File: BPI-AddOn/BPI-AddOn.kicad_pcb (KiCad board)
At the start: 2 copper layers, 100 x 100 mm, 81 parts, among them CON1 BARREL_JACK, J1 RJ45, J2 RJ45, J3 RJ45, P1 DIN10-1, P10 CONN_01X03, P11 CONN_01X05, P12 CONN_01X05, P13 CONN_01X08, P15 CONN_02X11, P16 USB_B, P17 CONN_01X05, P18 CONN_01X05, P19 V, P2 DIN10-2, P20 - +, P21 USB_OTG, P22 CONN_01X06, P23 CONN_01X06, P24 CONN_02X02, P25 CONN_01X02, P3 DIN10-3, P4 DIN10-4, P5 DIN10-5, P6 DIN7-1, P7 DIN7-2, P8 DIN7-3, P9 CONN_01X03, U1 MC34063, U2 FT230XS

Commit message: wip
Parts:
- added G***: LOGO, w_logo:Logo_copper_CC-BY-NC-SA_10x3.6mm, F.Cu at (91.5, 101.5)
- added G***: LOGO, w_logo:Logo_copper_CC-BY-NC-SA_10x3.6mm, F.Cu at (133.5, 113.5)
- added G***: LOGO, w_logo:Logo_copper_CC-BY-NC-SA_10x3.6mm, F.Cu at (160.0, 136.5)
- moved REF3 1.41 mm to (162.0, 144.0)
- moved REF4 1.41 mm to (127.0, 144.0)
- moved REF3 1.12 mm to (127.0, 129.0)
- moved REF4 1.12 mm to (162.0, 129.0)
- moved P21 0.50 mm to (144.5, 118.0)
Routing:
- net /GSB: track 0.00 -> 62.9 mm
- net VCC: track 130.6 -> 124.4 mm
- net /CANL: track 131.3 -> 126.7 mm
- net /CANH: track 133.9 -> 130.7 mm
- added copper zone on B.Cu, net GNDA
- added copper zone on F.Cu, net GNDA
- added copper zone on B.Cu, net GNDD
- added copper zone on F.Cu, net GNDD
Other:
- board text added: "Version 1.0 06/2016 Gerhard Bertelsmann"

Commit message: wip
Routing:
- net /GS0: track 45.8 -> 152.0 mm
- net /GSB: track 62.9 -> 141.9 mm
- net VCC: track 124.4 -> 176.6 mm
- net /CANH: track 130.7 -> 181.6 mm
- net /CANL: track 126.7 -> 175.9 mm
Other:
- net class Defaul_II: clearance 0.2 -> 0.4
- net class Default: clearance 0.2 -> 0.4
- rule trace_clearance: 0.2 -> 0.4

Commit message: route left part ...
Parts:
- CON1: value BARREL_JACK -> BJ
- moved F1 1.13 mm to (92.6, 68.0)
- moved D4 0.27 mm to (98.5, 83.2), turned to 90 degrees
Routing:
- net /CANH: track 181.6 -> 288.9 mm, vias 2 -> 11
- net /CANL: track 175.9 -> 256.0 mm, vias 2 -> 11
- net /5V: track 25.7 -> 102.8 mm, vias 0 -> 1
- net /GSB: track 141.9 -> 215.7 mm, vias 0 -> 1
- net /GS0: track 152.0 -> 219.6 mm, vias 0 -> 7
- net VCC: track 176.6 -> 239.6 mm, vias 1 -> 7
- net Net-(F2-Pad1): track 0.00 -> 25.4 mm, vias 0 -> 1
- net Net-(P19-Pad3): track 0.00 -> 18.7 mm
- net Net-(P16-Pad5): track 0.00 -> 16.6 mm, vias 0 -> 2
- net Net-(J2-Pad9): track 0.00 -> 15.5 mm
- net Net-(J1-Pad9): track 0.00 -> 15.5 mm
- net Net-(F1-Pad2): track 0.00 -> 14.2 mm
- net Net-(CON1-Pad3): track 0.00 -> 9.39 mm
- net /Vdd: track 0.00 -> 7.47 mm
- net Net-(P25-Pad1): track 0.00 -> 6.54 mm
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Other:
- net class Defaul_II: clearance 0.4 -> 0.2
- net class Default: clearance 0.4 -> 0.2
- rule trace_clearance: 0.4 -> 0.2
- board text added: "AK"
- board text added: "BJ"

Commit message: wip
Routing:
- net VCC: track 239.6 -> 261.5 mm, vias 7 -> 9
- net /GS0: track 219.6 -> 223.3 mm
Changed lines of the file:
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@@
-(kicad_pcb (version 4) (host pcbnew 4.0.2-stable)
+(kicad_pcb (version 4) (host pcbnew 4.0.1-stable)
   (general
     (links 233)
-    (no_connects 113)
-    (area 66.924999 48.924999 167.075001 149.075001)
+    (no_connects 140)
+    (area 64.132499 38.02446 183.5 159.200001)
     (thickness 1.6)
     (drawings 90)
-    (tracks 380)
+    (tracks 393)
     (zones 0)
     (modules 84)
@@
   (gr_line (start 69.5 149) (end 114.5 149) (angle 90) (layer Edge.Cuts) (width 0.15))
   (gr_line (start 69.5 49) (end 114.5 49) (angle 90) (layer Edge.Cuts) (width 0.15))
+  (segment (start 75.5 121.65) (end 79.1685 121.65) (width 0.6) (layer F.Cu) (net 1) (status 400000))
+  (segment (start 79.1685 121.65) (end 79.1845 121.666) (width 0.6) (layer F.Cu) (net 1))
   (segment (start 82.50249 73.063905) (end 82.50249 73.771011) (width 0.6) (layer F.Cu) (net 1))
   (segment (start 82.486589 66.431589) (end 82.486589 73.048004) (width 0.6) (layer F.Cu) (net 1))
@@
   (segment (start 96.6724 60.1599) (end 100.6729 56.1594) (width 1.2) (layer B.Cu) (net 11))
   (segment (start 95.0976 68.0466) (end 96.6724 66.4718) (width 1.2) (layer B.Cu) (net 11))
-  (segment (start 92.8878 70.739) (end 90.551 73.0758) (width 1.2) (layer F.Cu) (net 12))
-  (segment (start 90.551 73.0758) (end 90.551 87.0585) (width 1.2) (layer F.Cu) (net 12))
-  (segment (start 91.96 63) (end 91.96 69.8112) (width 1.2) (layer B.Cu) (net 12))
-  (segment (start 91.96 69.8112) (end 92.8878 70.739) (width 1.2) (layer B.Cu) (net 12))
-  (via (at 92.8878 70.739) (size 1.3) (drill 1) (layers F.Cu B.Cu) (net 12))
+  (segment (start 92.839655 69.337481) (end 93.489654 69.98748) (width 1.2) (layer B.Cu) (net 12))
+  (segment (start 91.96 63) (end 91.96 68.457826) (width 1.2) (layer B.Cu) (net 12))
+  (segment (start 92.839655 70.637479) (end 93.489654 69.98748) (width 1.2) (layer F.Cu) (net 12))
+  (segment (start 90.551 72.926134) (end 92.839655 70.637479) (width 1.2) (layer F.Cu) (net 12))
+  (segment (start 90.551 87.0585) (end 90.551 72.926134) (width 1.2) (layer F.Cu) (net 12))
+  (segment (start 91.96 68.457826) (end 92.839655 69.337481) (width 1.2) (layer B.Cu) (net 12))
+  (via (at 93.489654 69.98748) (size 1.3) (drill 1) (layers F.Cu B.Cu) (net 12))
   (segment (start 85.217 91.8845) (end 87.757 91.8845) (width 1.2) (layer B.Cu) (net 13))
   (segment (start 85.217 91.8845) (end 85.217 87.3125) (width 1.2) (layer B.Cu) (net 13))
@@
   (segment (start 152.78 134.72) (end 152.78 126.5) (width 0.6) (layer B.Cu) (net 20))
   (segment (start 150.38 137.12) (end 152.78 134.72) (width 0.6) (layer B.Cu) (net 20))
+  (segment (start 94.8055 71.4375) (end 94.8055 75.071022) (width 1.2) (layer F.Cu) (net 22))
+  (via (at 94.8055 75.071022) (size 1.3) (drill 1) (layers F.Cu B.Cu) (net 22))
+  (segment (start 94.8055 71.4375) (end 97.9805 71.4375) (width 1.2) (layer B.Cu) (net 22))
+  (segment (start 86.0439 71.4375) (end 94.8055 71.4375) (width 1.2) (layer B.Cu) (net 22))
+  (via (at 94.8055 71.4375) (size 1.3) (drill 1) (layers F.Cu B.Cu) (net 22))
+  (segment (start 97.9805 71.4375) (end 98.75 70.668) (width 1.2) (layer B.Cu) (net 22))
+  (segment (start 98.75 70.668) (end 98.75 68.58) (width 1.2) (layer B.Cu) (net 22))
+  (segment (start 85.25 68.58) (end 85.25 70.6436) (width 1.2) (layer B.Cu) (net 22))
+  (segment (start 85.25 70.6436) (end 86.0439 71.4375) (width 1.2) (layer B.Cu) (net 22))
   (segment (start 98.5012 83.185) (end 103.117233 83.185) (width 1.2) (layer F.Cu) (net 22))
   (segment (start 103.117233 83.185) (end 104.057033 82.2452) (width 1.2) (layer F.Cu) (net 22))

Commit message: wip
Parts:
- added P14: CONN_02X11, Pin_Headers:Pin_Header_Straight_2x11, F.Cu at (127.3, 85.5)
- CON1: value BJ -> BARREL_JACK
- moved C8 28.4 mm to (156.2, 103.9), turned to 0 degrees
- moved C9 26.0 mm to (156.2, 106.7), turned to 0 degrees
- moved U2 21.6 mm to (156.1, 111.0)
- moved R12 18.7 mm to (151.3, 112.3), turned to 90 degrees
- moved C5 10.5 mm to (149.7, 104.5)
- moved P23 10.4 mm to (125.5, 99.4)
- moved R10 7.04 mm to (152.9, 119.0), turned to 180 degrees
- moved R11 5.17 mm to (152.9, 115.8), turned to 180 degrees
- moved D2 4.47 mm to (157.7, 119.0), turned to 0 degrees
- moved G*** 1.76 mm to (133.0, 111.8)
- moved D3 1.41 mm to (157.7, 115.8), turned to 0 degrees
- moved E05 0.61 mm to (145.0, 120.0)
- moved E05 0.41 mm to (145.0, 122.5)
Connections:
- net /Vout renamed /21_15
- net Net-(P15-Pad1) renamed /21_01
- net Net-(P15-Pad3) renamed /21_02
- C2 pad 1: VCC -> VAA
- D4 pad 1: VCC -> /Vcc
- P1 pad 1: VCC -> /Vcc
- P1 pad 5: VCC -> /Vcc
- P10 pad 3: VCC -> /Vcc
- P11 pad 1: VCC -> /Vcc
- P12 pad 1: VCC -> /Vcc
- P15 pad 10: Net-(P15-Pad10) -> /21_17
- P15 pad 11: Net-(P15-Pad11) -> /21_06
- P15 pad 12: Net-(P15-Pad12) -> /21_16
- P15 pad 13: Net-(P15-Pad13) -> /21_07
- P15 pad 15: Net-(P15-Pad15) -> /21_08
- P15 pad 16: Net-(P15-Pad16) -> /21_14
- P15 pad 17: Net-(P15-Pad17) -> /21_09
- P15 pad 18: Net-(P15-Pad18) -> /21_13
- P15 pad 19: Net-(P15-Pad19) -> /21_10
- P15 pad 20: Net-(P15-Pad20) -> /21_12
- P15 pad 22: Net-(P15-Pad22) -> /21_11
- P15 pad 5: Net-(P15-Pad5) -> /21_03
- P15 pad 7: Net-(P15-Pad7) -> /21_04
- P15 pad 8: Net-(P15-Pad8) -> /21_18
- P15 pad 9: Net-(P15-Pad9) -> /21_05
- P17 pad 1: VCC -> /Vcc
- P18 pad 1: VCC -> /Vcc
- P2 pad 1: VCC -> /Vcc
- P2 pad 5: VCC -> /Vcc
- P22 pad 2: VCC -> VAA
- P23 pad 2: VCC -> VAA
- P3 pad 1: VCC -> /Vcc
- P3 pad 5: VCC -> /Vcc
- P4 pad 1: VCC -> /Vcc
- P4 pad 5: VCC -> /Vcc
- P5 pad 1: VCC -> /Vcc
- P5 pad 5: VCC -> /Vcc
- P6 pad 1: VCC -> /Vcc
- P7 pad 1: VCC -> /Vcc
- P8 pad 1: VCC -> /Vcc
- P9 pad 3: VCC -> /Vcc
- R4 pad 1: VCC -> VAA
- U1 pad 6: VCC -> VAA
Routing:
- net VCC: track 261.5 -> 0.00 mm, vias 9 -> 0
- net /Vcc: track 0.00 -> 261.5 mm, vias 0 -> 9
- net Net-(C4-Pad1): track 0.00 -> 7.51 mm, vias 0 -> 2
- net /GS0: track 223.3 -> 226.6 mm, vias 7 -> 9
- net /GSB: track 215.7 -> 217.9 mm
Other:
- outline, holes or cut-outs redrawn

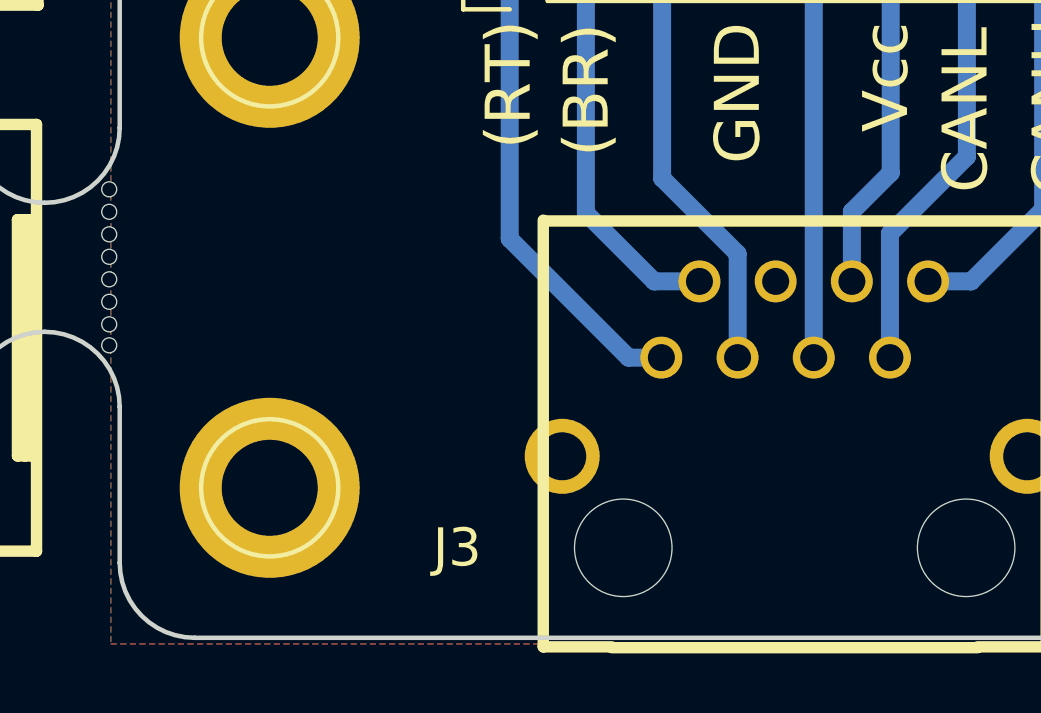
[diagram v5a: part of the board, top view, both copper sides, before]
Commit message: add LED for GLeisbox
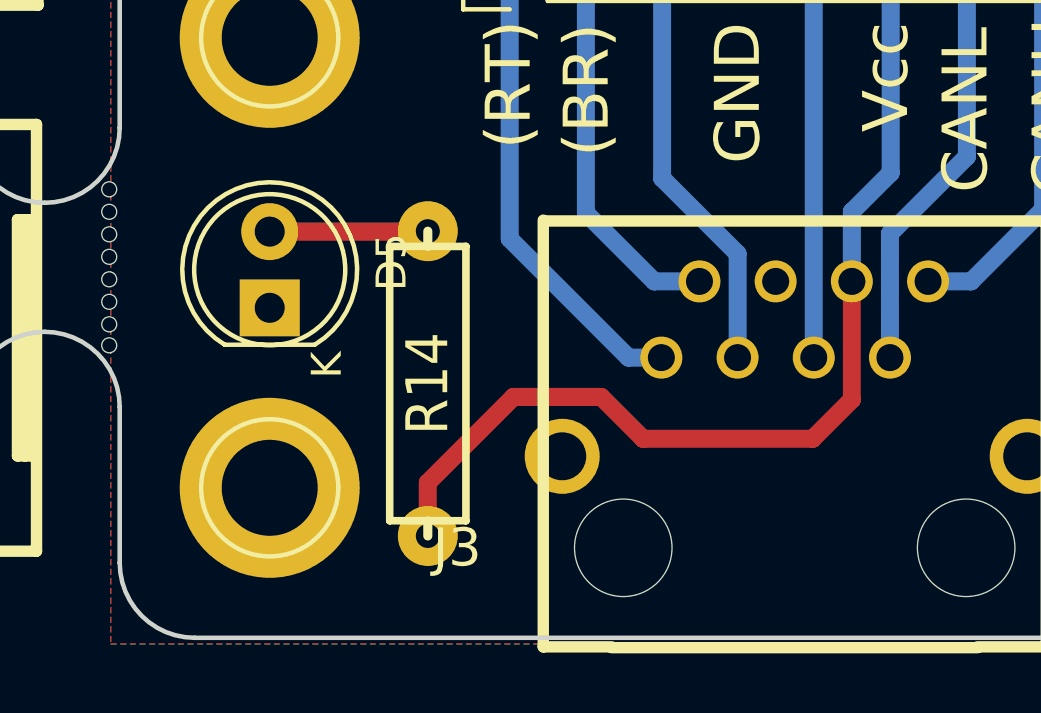
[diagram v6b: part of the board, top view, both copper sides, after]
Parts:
- added D5: LED, LEDs:LED-5MM, F.Cu at (127.0, 138.0)
- added R14: 10k, w_pth_resistors:RC05, F.Cu at (132.3, 140.5)
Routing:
- net Net-(J3-Pad6): track 11.2 -> 33.3 mm
- net Net-(D5-Pad2): track 0.00 -> 5.28 mm
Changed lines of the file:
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@@
-(kicad_pcb (version 4) (host pcbnew 4.0.2+e4-6225~38~ubuntu14.04.1-stable)
+(kicad_pcb (version 4) (host pcbnew 4.0.1-stable)
   (general
-    (links 253)
-    (no_connects 155)
+    (links 256)
+    (no_connects 80)
     (area 66.924999 48.924999 167.075001 149.075001)
     (thickness 1.6)
     (drawings 89)
-    (tracks 425)
+    (tracks 434)
     (zones 0)
-    (modules 85)
-    (nets 80)
+    (modules 87)
+    (nets 81)
   )
   (page A4)
@@
   (net 78 "Net-(P14-Pad21)")
   (net 79 /21_11)
+  (net 80 "Net-(D5-Pad2)")
   (net_class Default "This is the default net class."
     (clearance 0.2)
@@
     (add_net "Net-(D3-Pad1)")
     (add_net "Net-(D4-Pad2)")
+    (add_net "Net-(D5-Pad2)")
     (add_net "Net-(J1-Pad9)")
     (add_net "Net-(J2-Pad9)")
@@
     )
   )
+  (module LEDs:LED-5MM (layer F.Cu)
+    (at 127 138 90)
+    (descr "LED 5mm round vertical")
+    (tags "LED 5mm round vertical")
+    (fp_text reference D5 (at 1.524 4.064 90) (layer F.SilkS)
+      (effects (font (size 1 1) (thickness 0.15)))
+    )
+    (fp_text value LED (at 1.524 -3.937 90) (layer F.Fab)
+      (effects (font (size 1 1) (thickness 0.15)))
+    )
+    (fp_line (start -1.5 -1.55) (end -1.5 1.55) (layer F.CrtYd) (width 0.05))
+    (fp_arc (start 1.3 0) (end -1.5 1.55) (angle -302) (layer F.CrtYd) (width 0.05))
+    (fp_arc (start 1.27 0) (end -1.23 -1.5) (angle 297.5) (layer F.SilkS) (width 0.15))
+    (fp_line (start -1.23 1.5) (end -1.23 -1.5) (layer F.SilkS) (width 0.15))
+    (fp_circle (center 1.27 0) (end 0.97 -2.5) (layer F.SilkS) (width 0.15))
+    (fp_text user K (at -1.905 1.905 90) (layer F.SilkS)
+      (effects (font (size 1 1) (thickness 0.15)))
+    )
+    (pad 1 thru_hole rect (at 0 0 180) (size 2 1.9) (drill 1.00076) (layers *.Cu *.Mask F.SilkS)
+      (net 52 /GNDB))
+    (pad 2 thru_hole circle (at 2.54 0 90) (size 1.9 1.9) (drill 1.00076) (layers *.Cu *.Mask F.SilkS)
+      (net 80 "Net-(D5-Pad2)"))
+    (model LEDs.3dshapes/LED-5MM.wrl
+      (at (xyz 0.05 0 0))
+      (scale (xyz 1 1 1))
+      (rotate (xyz 0 0 90))
+    )
+  )
+  (module w_pth_resistors:RC05 (layer F.Cu)
+    (at 132.2705 140.5255 270)
+    (descr "Resistor, RC05")
+    (tags R)
+    (autoplace_cost180 10)
+    (fp_text reference R14 (at 0 0 270) (layer F.SilkS)
+      (effects (font (size 1.397 1.27) (thickness 0.2032)))
+    )
+    (fp_text value 10k (at 0 2.032 270) (layer F.SilkS) hide
+      (effects (font (size 1.397 1.27) (thickness 0.2032)))
+    )
+    (fp_line (start 4.572 1.27) (end -4.572 1.27) (layer F.SilkS) (width 0.254))
+    (fp_line (start -4.572 1.27) (end -4.572 -1.27) (layer F.SilkS) (width 0.254))
+    (fp_line (start -4.572 -1.27) (end 4.572 -1.27) (layer F.SilkS) (width 0.254))
+    (fp_line (start 4.572 -1.27) (end 4.572 1.27) (layer F.SilkS) (width 0.254))
+    (fp_line (start -5.08 0) (end -4.572 0) (layer F.SilkS) (width 0.3048))
+    (fp_line (start 5.08 0) (end 4.572 0) (layer F.SilkS) (width 0.3048))
+    (pad 1 thru_hole circle (at -5.08 0 270) (size 1.99898 1.99898) (drill 0.8001) (layers *.Cu *.Mask F.SilkS)
+      (net 80 "Net-(D5-Pad2)"))
+    (pad 2 thru_hole circle (at 5.08 0 270) (size 1.99898 1.99898) (drill 0.8001) (layers *.Cu *.Mask F.SilkS)
+      (net 18 "Net-(J3-Pad6)"))
+    (model walter/pth_resistors/rc05.wrl
+      (at (xyz 0 0 0))
+      (scale (xyz 1 1 1))
+      (rotate (xyz 0 0 0))
+    )
+  )
   (dimension 25 (width 0.3) (layer Dwgs.User)
     (gr_text "25.000 mm" (at 175.85 136.5 90) (layer Dwgs.User)
@@
   (segment (start 145.135 139.66) (end 145.135 126.525) (width 0.6) (layer B.Cu) (net 17))
   (segment (start 145.135 126.525) (end 145.16 126.5) (width 0.6) (layer B.Cu) (net 17))
+  (segment (start 132.2705 145.6055) (end 132.2705 143.8275) (width 0.6) (layer F.Cu) (net 18) (status 400000))
+  (segment (start 146.405 141.0595) (end 146.405 137.12) (width 0.6) (layer F.Cu) (net 18) (status 800000))
+  (segment (start 145.0975 142.367) (end 146.405 141.0595) (width 0.6) (layer F.Cu) (net 18))
+  (segment (start 139.446 142.367) (end 145.0975 142.367) (width 0.6) (layer F.Cu) (net 18))
+  (segment (start 138.049 140.97) (end 139.446 142.367) (width 0.6) (layer F.Cu) (net 18))
+  (segment (start 135.128 140.97) (end 138.049 140.97) (width 0.6) (layer F.Cu) (net 18))
+  (segment (start 132.2705 143.8275) (end 135.128 140.97) (width 0.6) (layer F.Cu) (net 18))
   (segment (start 146.405 137.12) (end 146.405 134.795) (width 0.6) (layer B.Cu) (net 18))
   (segment (start 147.7 133.5) (end 147.7 126.5) (width 0.6) (layer B.Cu) (net 18))
@@
   (segment (start 98.9024 68.58) (end 98.75 68.58) (width 1.2) (layer B.Cu) (net 60))
   (segment (start 98 133.5) (end 98.25 133.25) (width 0.6) (layer B.Cu) (net 60))
+  (segment (start 127 135.46) (end 132.256 135.46) (width 0.6) (layer F.Cu) (net 80) (status C00000))
+  (segment (start 132.256 135.46) (end 132.2705 135.4455) (width 0.6) (layer F.Cu) (net 80) (status C00000))
   (zone (net 52) (net_name /GNDB) (layer F.Cu) (hatch edge 0.508)
     (connect_pads (clearance 0.254))
     (min_thickness 0.254)
-    (fill (arc_segments 16) (thermal_gap 0.508) (thermal_bridge_width 0.508))
+    (fill yes (arc_segments 16) (thermal_gap 0.508) (thermal_bridge_width 0.508))
     (polygon
       (pts
@@
     (connect_pads (clearance 0.254))
     (min_thickness 0.254)
-    (fill (arc_segments 16) (thermal_gap 0.508) (thermal_bridge_width 0.508))
+    (fill yes (arc_segments 16) (thermal_gap 0.508) (thermal_bridge_width 0.508))
     (polygon
       (pts
@@
     (connect_pads (clearance 0.254))
     (min_thickness 0.254)
-    (fill (arc_segments 16) (thermal_gap 0.508) (thermal_bridge_width 0.508))
+    (fill yes (arc_segments 16) (thermal_gap 0.508) (thermal_bridge_width 0.508))
     (polygon
       (pts
@@
     (connect_pads (clearance 0.254))
     (min_thickness 0.254)
-    (fill (arc_segments 16) (thermal_gap 0.508) (thermal_bridge_width 0.508))
+    (fill yes (arc_segments 16) (thermal_gap 0.508) (thermal_bridge_width 0.508))
     (polygon
       (pts
@@
     (connect_pads (clearance 0.254))
     (min_thickness 0.254)
-    (fill (arc_segments 16) (thermal_gap 0.508) (thermal_bridge_width 0.508))
+    (fill yes (arc_segments 16) (thermal_gap 0.508) (thermal_bridge_width 0.508))
     (polygon
       (pts
@@
     (connect_pads (clearance 0.254))
     (min_thickness 0.254)
-    (fill (arc_segments 16) (thermal_gap 0.508) (thermal_bridge_width 0.508))
+    (fill yes (arc_segments 16) (thermal_gap 0.508) (thermal_bridge_width 0.508))
     (polygon
       (pts

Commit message: wip
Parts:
- added P26: CONN_01X03, Pin_Headers:Pin_Header_Straight_1x03, F.Cu at (140.2, 80.3)
- added P27: CONN_01X04, Pin_Headers:Pin_Header_Straight_1x04, F.Cu at (130.6, 76.4)
- added P28: CONN_01X03, Pin_Headers:Pin_Header_Straight_1x03, F.Cu at (134.9, 102.0)
- added Q1: BS170, w_to:to92_3_flat, F.Cu at (149.2, 68.3)
- added Q2: BS170, w_to:to92_3_flat, F.Cu at (153.4, 71.1)
- added Q3: BS170, w_to:to92_3_flat, F.Cu at (149.2, 74.0)
- added Q4: BS170, w_to:to92_3_flat, F.Cu at (152.9, 77.5)
- added R15: 4k7, w_pth_resistors:RC03, F.Cu at (141.5, 68.6)
- added R16: 4k7, w_pth_resistors:RC03, F.Cu at (141.5, 71.3)
- added R17: 4k7, w_pth_resistors:RC03, F.Cu at (159.4, 68.6)
- added R18: 4k7, w_pth_resistors:RC03, F.Cu at (159.4, 71.2)
- added R19: 4k7, w_pth_resistors:RC03, F.Cu at (141.5, 73.9)
- added R20: 4k7, w_pth_resistors:RC03, F.Cu at (141.7, 76.6)
- added R21: 4k7, w_pth_resistors:RC03, F.Cu at (159.4, 73.7)
- added R22: 4k7, w_pth_resistors:RC03, F.Cu at (159.4, 76.5)
- moved R5 31.1 mm to (149.2, 99.8)
- moved R7 19.7 mm to (139.3, 95.8), turned to 90 degrees
- moved R4 17.3 mm to (149.2, 97.2)
- moved R6 12.3 mm to (143.1, 86.7)
- moved U1 10.8 mm to (149.2, 92.1), turned to 180 degrees
- moved P24 10.2 mm to (155.7, 82.2)
- moved C2 7.77 mm to (143.8, 91.7)
- moved D1 7.46 mm to (139.0, 83.4), turned to 0 degrees
- moved C1 6.69 mm to (150.6, 86.0)
- moved C3 4.50 mm to (135.2, 88.8), turned to 180 degrees
- moved L1 3.85 mm to (159.8, 89.4), turned to 90 degrees
- moved P15 2.64 mm to (134.9, 56.9)
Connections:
- net Net-(C5-Pad1) renamed /Vccio
- net Net-(C8-Pad1) renamed /Vusb
- C2 pad 1: VAA -> /Vin
- P24 pad 2: /RxD -> /_RxD
- P24 pad 3: /TxD -> /_TxD
- R4 pad 1: VAA -> /Vin
- R5 pad 1: Net-(L1-Pad1) -> Net-(R5-Pad1)
- R5 pad 2: Net-(R5-Pad2) -> Net-(L1-Pad1)
- U1 pad 6: VAA -> /Vin
- U1 pad 8: Net-(R5-Pad2) -> Net-(R5-Pad1)

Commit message: wip
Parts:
- added P29: CONN_01X01, Pin_Headers:Pin_Header_Straight_1x01, F.Cu at (176.4, 87.9)
- added R23: R, w_pth_resistors:RC03, F.Cu at (186.2, 92.3)
- added R24: R, w_pth_resistors:RC03, F.Cu at (186.0, 97.1)
- added R25: R, w_pth_resistors:RC03, F.Cu at (185.6, 100.8)
- R15, R16, R17, R18, R19, R20, R21, R22: footprint w_pth_resistors:RC03 -> Resistors_SMD:R_0805_HandSoldering
- moved P24 27.2 mm to (128.5, 82.7)
- moved C4 11.4 mm to (138.5, 108.5), turned to 270 degrees
- moved P14 11.0 mm to (133.9, 76.7)
- moved P27 4.81 mm to (125.9, 77.2)
- moved P15 4.79 mm to (139.7, 56.9)
- moved D1 3.15 mm to (136.6, 85.5)
- moved C3 2.86 mm to (135.0, 91.7), turned to 0 degrees
- moved P22 2.82 mm to (165.2, 99.8)
- moved R16 2.77 mm to (144.3, 70.9)
- moved R19 2.70 mm to (144.2, 74.3)
- moved R15 2.58 mm to (144.1, 68.5)
- moved R20 2.55 mm to (144.2, 76.6)
- moved R22 2.53 mm to (156.9, 76.3)
- moved R21 2.52 mm to (156.9, 74.1)
- moved R18 2.38 mm to (157.1, 70.7)
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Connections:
- P24 pad 2: /_RxD -> Net-(P24-Pad2)
- P24 pad 3: /_TxD -> Net-(P24-Pad3)
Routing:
- net /Vusb: track 0.00 -> 37.1 mm, vias 0 -> 4
- net /21_15: track 0.00 -> 30.0 mm
- net /Vccio: track 0.00 -> 24.9 mm
- net /Vin: track 0.00 -> 24.5 mm
- net Net-(R9-Pad1): track 0.00 -> 21.7 mm
- net Net-(D1-Pad2): track 0.00 -> 21.5 mm, vias 0 -> 1
- net Net-(L1-Pad1): track 0.00 -> 20.1 mm
- net Net-(R8-Pad2): track 0.00 -> 17.0 mm, vias 0 -> 2
- net /21_07: track 0.00 -> 15.8 mm, vias 0 -> 1
- net /21_08: track 0.00 -> 15.1 mm, vias 0 -> 1
- net /21_18: track 0.00 -> 14.3 mm
- net /21_16: track 0.00 -> 13.9 mm, vias 0 -> 2
- net /21_09: track 0.00 -> 13.7 mm, vias 0 -> 1
- net /21_10: track 0.00 -> 13.2 mm, vias 0 -> 1
- net Net-(R11-Pad2): track 0.00 -> 11.8 mm, vias 0 -> 2
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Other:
- board text added: "CTS"
- board text added: "RTS"
- board text added: "RxD"
- board text added: "TxD"
- board text added: "Vaa"
